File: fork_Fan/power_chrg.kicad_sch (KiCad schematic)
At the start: 32 parts, among them J1 Conn_01x02, J2 USB_C_Receptacle_PowerOnly_6P, Q1 Q_NMOS, U1 CS5086E, U2 HT7150-1

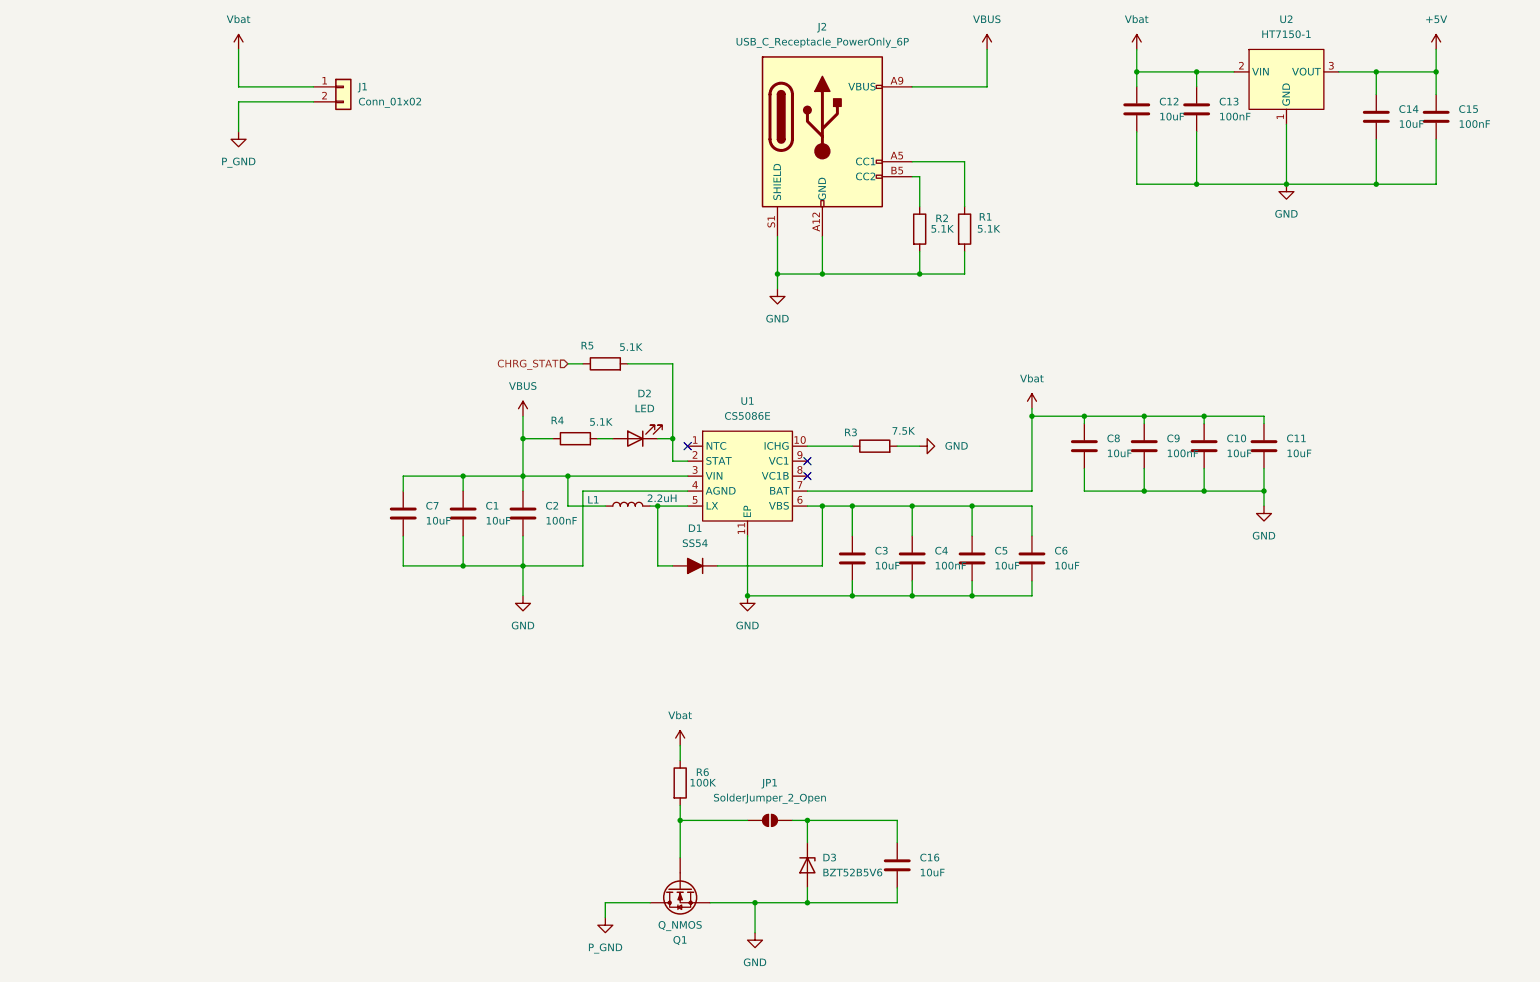
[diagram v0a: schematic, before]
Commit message: add mcu and some motor driver need bat sample, key, programing pad, fuse, fd6288 power.
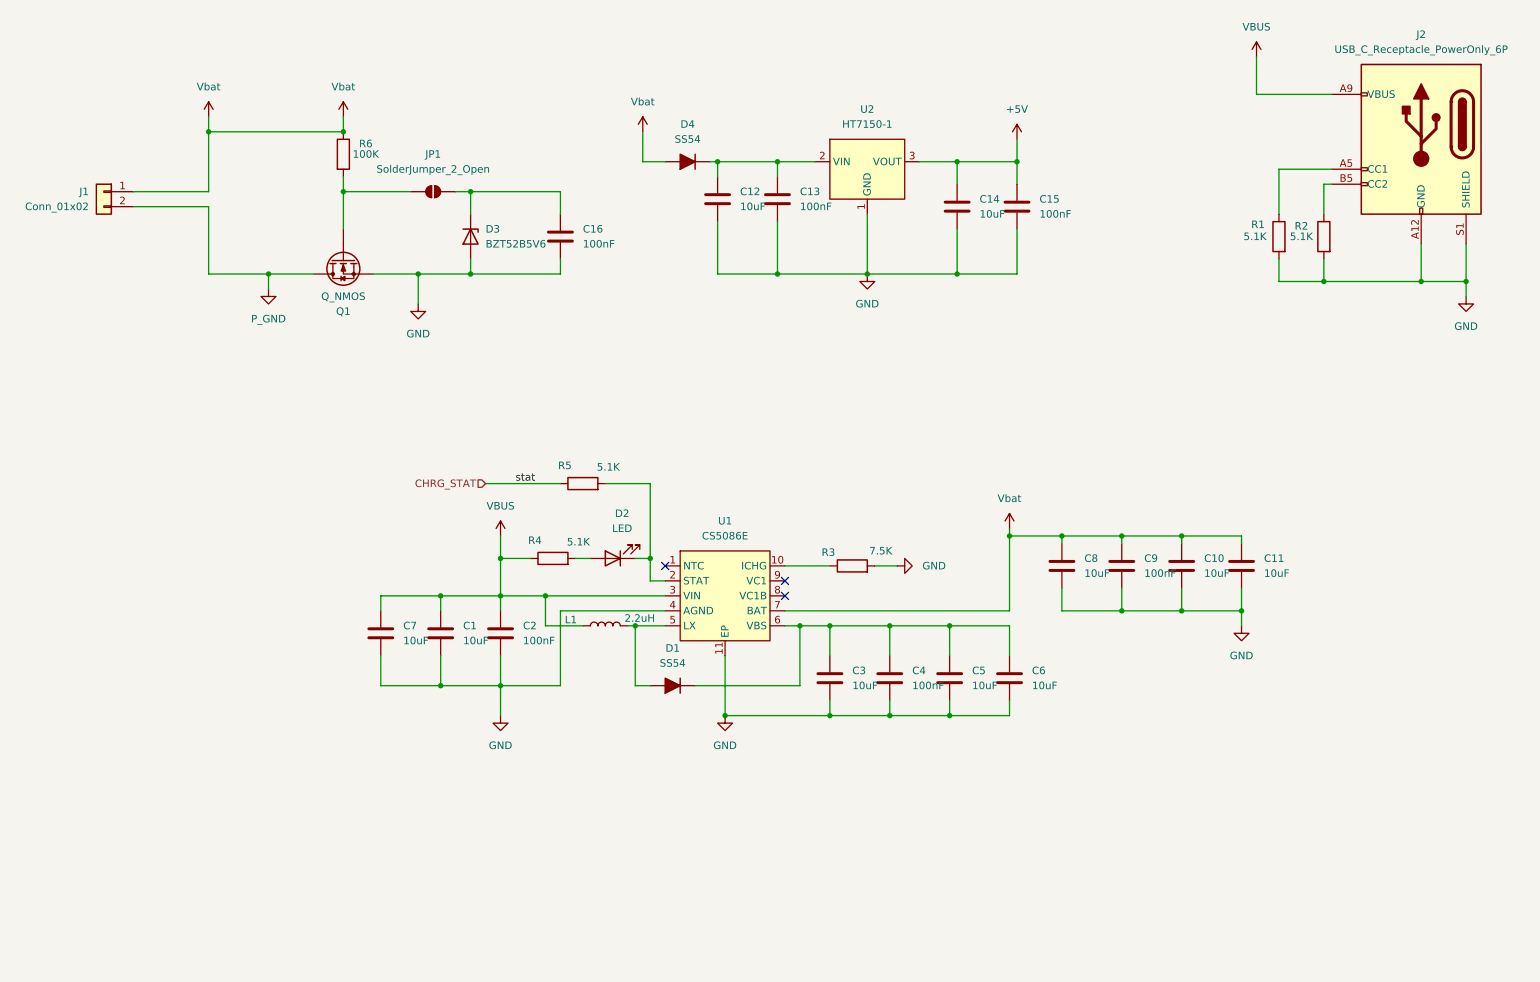
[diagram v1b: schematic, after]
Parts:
- added D4: SS54, Diode_SMD:D_SMA, symbol Device:D_Filled
- C16: value 10uF -> 100nF
- Q1: footprint me_Lib:PQFN-8_L6.0-W5.0-P1.27-LS6.0-BL_DSG -> me_Lib:PDFN-8_L3.3-W3.3-P0.65-BL-DSG
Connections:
- net Vbat: now also D4.2 (A); no longer C12.1, C13.1, U2.2 (VIN)
- new net: C12.1, C13.1, D4.1 (K), U2.2 (VIN)
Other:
- moved on the sheet: C1, C10, C11, C12, C13, C14, C15, C16, C2, C3, C4, C5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

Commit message: fix code
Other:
- note added: "改dcdc"
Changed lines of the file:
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@@
 	(generator_version "9.0")
 	(paper "A4")
+	(text "改dcdc\n"
+		(exclude_from_sim no)
+		(at 163.83 34.29 0)
+		(effects
+			(font
+				(size 1.27 1.27)
+			)
+		)
+	)
 	(junction
 		(at 171.45 142.24)
